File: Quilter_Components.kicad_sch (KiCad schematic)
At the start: 38 parts, among them J1 Conn_01x10_Male, J2 Conn_01x10_Male, J3 Conn_01x10_Male, J4 Eurorack_10_pin_power, U1 TL072, U2 TL074, U3 TL074, U4 TL074

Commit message: Draft of 8HP component PCB routed
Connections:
- net AUDIO_BUFF3: now also J1.3 (Pin_3); no longer J2.2 (Pin_2)
- net AUDIO_BUFF4: now also J2.5 (Pin_5); no longer J1.8 (Pin_8)
- net AUDIO_IN4: now also J3.1 (Pin_1); no longer J3.5 (Pin_5)
- net FREQ_CV1: now also J3.7 (Pin_7); no longer J3.6 (Pin_6)
- net FREQ_CV4: now also J3.6 (Pin_6); no longer J3.3 (Pin_3)
- net FREQ_POT: now also J3.5 (Pin_5); no longer J3.7 (Pin_7)
- net FREQ_V_OCT2: now also J1.7 (Pin_7); no longer J2.4 (Pin_4)
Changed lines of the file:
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@@
     (effects (font (size 1.27 1.27)) (justify right bottom))
   )
-  (label "FREQ_V_OCT2" (at 56.515 95.885 0)
+  (label "FREQ_V_OCT2" (at 29.21 103.505 0)
     (effects (font (size 1.27 1.27)) (justify left bottom))
   )
@@
     (effects (font (size 1.27 1.27)) (justify right bottom))
   )
-  (label "AUDIO_IN4" (at 88.9 97.155 0)
+  (label "AUDIO_IN4" (at 88.9 86.995 0)
     (effects (font (size 1.27 1.27)) (justify left bottom))
   )
@@
     (effects (font (size 1.27 1.27)) (justify right bottom))
   )
-  (label "FREQ_CV1" (at 88.9 99.695 0)
+  (label "FREQ_CV1" (at 88.9 102.235 0)
     (effects (font (size 1.27 1.27)) (justify left bottom))
   )
@@
     (effects (font (size 1.27 1.27)) (justify left bottom))
   )
-  (label "AUDIO_BUFF3" (at 56.515 90.805 0)
+  (label "AUDIO_BUFF3" (at 29.21 93.345 0)
     (effects (font (size 1.27 1.27)) (justify left bottom))
   )
@@
     (effects (font (size 1.27 1.27)) (justify right bottom))
   )
-  (label "AUDIO_BUFF4" (at 29.21 106.045 0)
+  (label "AUDIO_BUFF4" (at 56.515 98.425 0)
     (effects (font (size 1.27 1.27)) (justify left bottom))
   )
-  (label "FREQ_CV4" (at 88.9 92.075 0)
+  (label "FREQ_CV4" (at 88.9 99.695 0)
     (effects (font (size 1.27 1.27)) (justify left bottom))
   )
@@
     (effects (font (size 1.27 1.27)) (justify left bottom))
   )
-  (label "FREQ_POT" (at 88.9 102.235 0)
+  (label "FREQ_POT" (at 88.9 97.155 0)
     (effects (font (size 1.27 1.27)) (justify left bottom))
   )

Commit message: First draft routing of Controls PCB
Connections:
- net +12V: now also J2.1 (Pin_1)
- net -12V: now also J1.1 (Pin_1)
- net AUDIO_IN2: now also J2.10 (Pin_10); no longer J2.9 (Pin_9)
- net FREQ_POT_5V: now also J2.7 (Pin_7); no longer J2.10 (Pin_10)
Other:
- moved on the sheet: J3
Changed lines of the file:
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@@
     (effects (font (size 1.27 1.27)) (justify right bottom))
   )
-  (label "FREQ_POT_5V" (at 56.515 111.125 0)
+  (label "FREQ_POT_5V" (at 56.515 103.505 0)
     (effects (font (size 1.27 1.27)) (justify left bottom))
   )
@@
     (effects (font (size 1.27 1.27)) (justify left bottom))
   )
-  (label "AUDIO_IN3" (at 88.9 107.315 0)
+  (label "AUDIO_IN3" (at 86.995 108.585 0)
     (effects (font (size 1.27 1.27)) (justify left bottom))
   )
@@
     (effects (font (size 1.27 1.27)) (justify right bottom))
   )
-  (label "AUDIO_IN4" (at 88.9 86.995 0)
+  (label "AUDIO_IN4" (at 86.995 88.265 0)
     (effects (font (size 1.27 1.27)) (justify left bottom))
   )
@@
     (effects (font (size 1.27 1.27)) (justify right bottom))
   )
-  (label "FREQ_V_OCT4" (at 88.9 89.535 0)
-    (effects (font (size 1.27 1.27)) (justify left bottom))
-  )
-  (label "FREQ_CV3" (at 88.9 104.775 0)
+  (label "FREQ_V_OCT4" (at 86.995 90.805 0)
+    (effects (font (size 1.27 1.27)) (justify left bottom))
+  )
+  (label "FREQ_CV3" (at 86.995 106.045 0)
     (effects (font (size 1.27 1.27)) (justify left bottom))
   )
@@
     (effects (font (size 1.27 1.27)) (justify left bottom))
   )
-  (label "AUDIO_IN2" (at 56.515 108.585 0)
+  (label "AUDIO_IN2" (at 56.515 111.125 0)
     (effects (font (size 1.27 1.27)) (justify left bottom))
   )
@@
     (effects (font (size 1.27 1.27)) (justify right bottom))
   )
-  (label "FREQ_CV1" (at 88.9 102.235 0)
+  (label "FREQ_CV1" (at 86.995 103.505 0)
     (effects (font (size 1.27 1.27)) (justify left bottom))
   )
@@
     (effects (font (size 1.27 1.27)) (justify right bottom))
   )
-  (label "Q_POT" (at 88.9 94.615 0)
+  (label "Q_POT" (at 86.995 95.885 0)
     (effects (font (size 1.27 1.27)) (justify left bottom))
   )
@@
     (effects (font (size 1.27 1.27)) (justify left bottom))
   )
-  (label "FREQ_CV4" (at 88.9 99.695 0)
+  (label "FREQ_CV4" (at 86.995 100.965 0)
     (effects (font (size 1.27 1.27)) (justify left bottom))
   )
@@
     (effects (font (size 1.27 1.27)) (justify right bottom))
   )
-  (label "FREQ_V_OCT3" (at 88.9 109.855 0)
+  (label "FREQ_V_OCT3" (at 86.995 111.125 0)
     (effects (font (size 1.27 1.27)) (justify left bottom))
   )
@@
     (effects (font (size 1.27 1.27)) (justify left bottom))
   )
-  (label "FREQ_POT" (at 88.9 97.155 0)
+  (label "FREQ_POT" (at 86.995 98.425 0)
     (effects (font (size 1.27 1.27)) (justify left bottom))
   )
@@
     (pin "8")
   )
+  (symbol (lib_id "power:+12V") (at 56.515 88.265 270) (unit 1)
+    (in_bom yes) (on_board yes) (fields_autoplaced)
+    (property "Reference" "#PWR0110" (id 0) (at 52.705 88.265 0)
+      (effects (font (size 1.27 1.27)) hide)
+    )
+    (property "Value" "+12V" (id 1) (at 60.9143 88.2649 90)
+      (effects (font (size 1.27 1.27)) (justify left))
+    )
+    (property "Footprint" "" (id 2) (at 56.515 88.265 0)
+      (effects (font (size 1.27 1.27)) hide)
+    )
+    (property "Datasheet" "" (id 3) (at 56.515 88.265 0)
+      (effects (font (size 1.27 1.27)) hide)
+    )
+    (pin "1")
+  )
   (symbol (lib_id "Connector:TestPoint") (at 163.195 169.545 90) (unit 1)
     (in_bom yes) (on_board yes)
@@
     )
     (property "Datasheet" "~" (id 3) (at 163.195 164.465 0)
+      (effects (font (size 1.27 1.27)) hide)
+    )
+    (pin "1")
+  )
+  (symbol (lib_id "power:-12V") (at 29.21 88.265 270) (unit 1)
+    (in_bom yes) (on_board yes) (fields_autoplaced)
+    (property "Reference" "#PWR0109" (id 0) (at 31.75 88.265 0)
+      (effects (font (size 1.27 1.27)) hide)
+    )
+    (property "Value" "-12V" (id 1) (at 33.02 88.2649 90)
+      (effects (font (size 1.27 1.27)) (justify left))
+    )
+    (property "Footprint" "" (id 2) (at 29.21 88.265 0)
+      (effects (font (size 1.27 1.27)) hide)
+    )
+    (property "Datasheet" "" (id 3) (at 29.21 88.265 0)
       (effects (font (size 1.27 1.27)) hide)
     )
@@
   )
   (symbol (lib_id "Connector:Conn_01x10_Male") (at 51.435 98.425 0) (unit 1)
-    (in_bom yes) (on_board yes) (fields_autoplaced)
-    (property "Reference" "J2" (id 0) (at 52.07 82.55 0))
-    (property "Value" "Conn_01x10_Male" (id 1) (at 52.07 85.09 0))
+    (in_bom yes) (on_board yes)
+    (property "Reference" "J2" (id 0) (at 58.42 81.915 0))
+    (property "Value" "Conn_01x10_Male" (id 1) (at 59.055 85.09 0))
     (property "Footprint" "Connector_PinHeader_2.54mm:PinHeader_1x10_P2.54mm_Vertical" (id 2) (at 51.435 98.425 0)
       (effects (font (size 1.27 1.27)) hide)
@@
   )
   (symbol (lib_id "Connector:Conn_01x10_Male") (at 24.13 98.425 0) (unit 1)
-    (in_bom yes) (on_board yes) (fields_autoplaced)
-    (property "Reference" "J1" (id 0) (at 24.765 82.55 0))
-    (property "Value" "Conn_01x10_Male" (id 1) (at 24.765 85.09 0))
+    (in_bom yes) (on_board yes)
+    (property "Reference" "J1" (id 0) (at 27.94 81.915 0))
+    (property "Value" "Conn_01x10_Male" (id 1) (at 31.75 85.09 0))
     (property "Footprint" "Connector_PinHeader_2.54mm:PinHeader_1x10_P2.54mm_Vertical" (id 2) (at 24.13 98.425 0)
       (effects (font (size 1.27 1.27)) hide)
@@
     (pin "1")
   )
-  (symbol (lib_id "Connector:Conn_01x10_Male") (at 83.82 97.155 0) (unit 1)
-    (in_bom yes) (on_board yes) (fields_autoplaced)
-    (property "Reference" "J3" (id 0) (at 84.455 81.28 0))
-    (property "Value" "Conn_01x10_Male" (id 1) (at 84.455 83.82 0))
-    (property "Footprint" "Connector_PinHeader_2.54mm:PinHeader_1x10_P2.54mm_Vertical" (id 2) (at 83.82 97.155 0)
-      (effects (font (size 1.27 1.27)) hide)
-    )
-    (property "Datasheet" "~" (id 3) (at 83.82 97.155 0)
+  (symbol (lib_id "Connector:Conn_01x10_Male") (at 81.915 98.425 0) (unit 1)
+    (in_bom yes) (on_board yes)
+    (property "Reference" "J3" (id 0) (at 90.17 81.915 0))
+    (property "Value" "Conn_01x10_Male" (id 1) (at 90.17 84.455 0))
+    (property "Footprint" "Connector_PinHeader_2.54mm:PinHeader_1x10_P2.54mm_Vertical" (id 2) (at 81.915 98.425 0)
+      (effects (font (size 1.27 1.27)) hide)
+    )
+    (property "Datasheet" "~" (id 3) (at 81.915 98.425 0)
       (effects (font (size 1.27 1.27)) hide)
     )
@@
       (reference "#PWR0108") (unit 1) (value "GND") (footprint "")
     )
+    (path "/1aaa51bf-e78e-45fa-8100-3ef683a49ac4"
+      (reference "#PWR0109") (unit 1) (value "-12V") (footprint "")
+    )
+    (path "/0fd6de80-7cc0-4387-a408-b278fa25950a"
+      (reference "#PWR0110") (unit 1) (value "+12V") (footprint "")
+    )
     (path "/2c333ca4-0780-4b24-87eb-2f414d90e6bb"

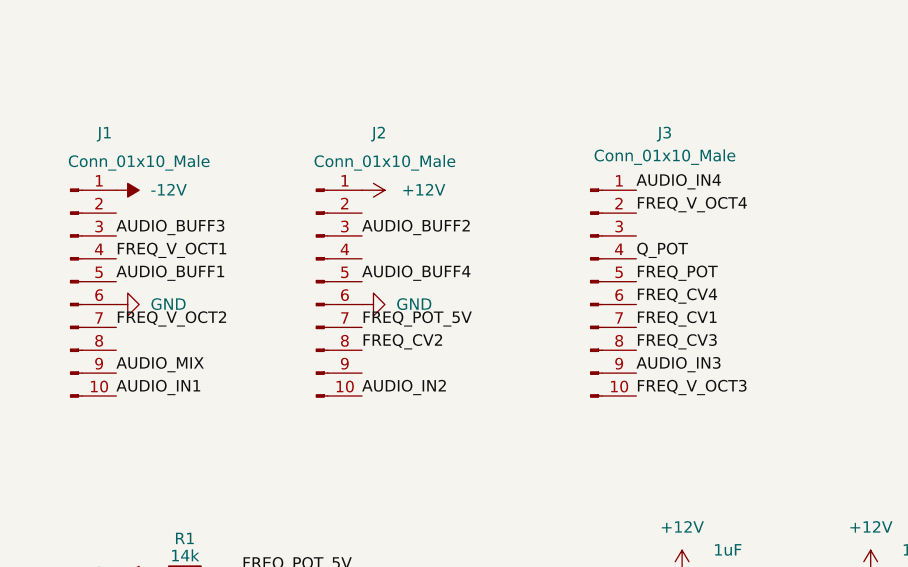
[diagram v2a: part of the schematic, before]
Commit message: Re-routed Controls board
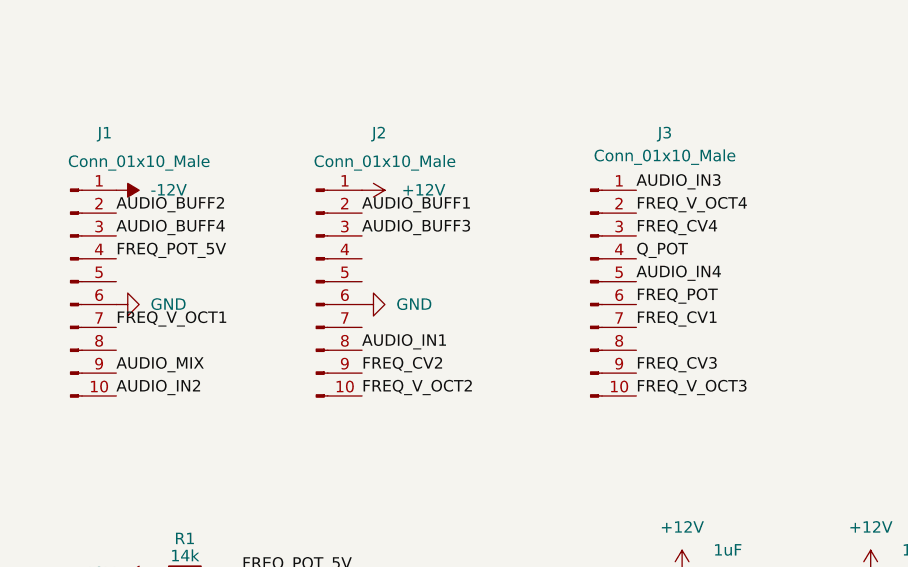
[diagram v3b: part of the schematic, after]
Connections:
- net AUDIO_BUFF1: now also J2.2 (Pin_2); no longer J1.5 (Pin_5)
- net AUDIO_BUFF2: now also J1.2 (Pin_2); no longer J2.3 (Pin_3)
- net AUDIO_BUFF3: now also J2.3 (Pin_3); no longer J1.3 (Pin_3)
- net AUDIO_BUFF4: now also J1.3 (Pin_3); no longer J2.5 (Pin_5)
- net AUDIO_IN1: now also J2.8 (Pin_8); no longer J1.10 (Pin_10)
- net AUDIO_IN2: now also J1.10 (Pin_10); no longer J2.10 (Pin_10)
- net AUDIO_IN3: now also J3.1 (Pin_1); no longer J3.9 (Pin_9)
- net AUDIO_IN4: now also J3.5 (Pin_5); no longer J3.1 (Pin_1)
- net FREQ_CV2: now also J2.9 (Pin_9); no longer J2.8 (Pin_8)
- net FREQ_CV3: now also J3.9 (Pin_9); no longer J3.8 (Pin_8)
- net FREQ_CV4: now also J3.3 (Pin_3); no longer J3.6 (Pin_6)
- net FREQ_POT: now also J3.6 (Pin_6); no longer J3.5 (Pin_5)
- net FREQ_POT_5V: now also J1.4 (Pin_4); no longer J2.7 (Pin_7)
- net FREQ_V_OCT1: now also J1.7 (Pin_7); no longer J1.4 (Pin_4)
- net FREQ_V_OCT2: now also J2.10 (Pin_10); no longer J1.7 (Pin_7)
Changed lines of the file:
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@@
     (effects (font (size 1.27 1.27)) (justify right bottom))
   )
-  (label "FREQ_POT_5V" (at 56.515 103.505 0)
+  (label "FREQ_POT_5V" (at 29.21 95.885 0)
     (effects (font (size 1.27 1.27)) (justify left bottom))
   )
@@
     (effects (font (size 1.27 1.27)) (justify right bottom))
   )
-  (label "FREQ_V_OCT2" (at 29.21 103.505 0)
+  (label "FREQ_V_OCT2" (at 56.515 111.125 0)
     (effects (font (size 1.27 1.27)) (justify left bottom))
   )
-  (label "AUDIO_IN3" (at 86.995 108.585 0)
+  (label "AUDIO_IN3" (at 86.995 88.265 0)
     (effects (font (size 1.27 1.27)) (justify left bottom))
   )
@@
     (effects (font (size 1.27 1.27)) (justify right bottom))
   )
-  (label "AUDIO_IN4" (at 86.995 88.265 0)
+  (label "AUDIO_IN4" (at 86.995 98.425 0)
     (effects (font (size 1.27 1.27)) (justify left bottom))
   )
@@
     (effects (font (size 1.27 1.27)) (justify left bottom))
   )
-  (label "FREQ_CV3" (at 86.995 106.045 0)
+  (label "FREQ_CV3" (at 86.995 108.585 0)
     (effects (font (size 1.27 1.27)) (justify left bottom))
   )
@@
     (effects (font (size 1.27 1.27)) (justify right bottom))
   )
-  (label "AUDIO_BUFF2" (at 56.515 93.345 0)
+  (label "AUDIO_BUFF2" (at 29.21 90.805 0)
     (effects (font (size 1.27 1.27)) (justify left bottom))
   )
@@
     (effects (font (size 1.27 1.27)) (justify right bottom))
   )
-  (label "AUDIO_BUFF1" (at 29.21 98.425 0)
+  (label "AUDIO_BUFF1" (at 56.515 90.805 0)
     (effects (font (size 1.27 1.27)) (justify left bottom))
   )
-  (label "AUDIO_IN2" (at 56.515 111.125 0)
+  (label "AUDIO_IN2" (at 29.21 111.125 0)
     (effects (font (size 1.27 1.27)) (justify left bottom))
   )
-  (label "FREQ_CV2" (at 56.515 106.045 0)
+  (label "FREQ_CV2" (at 56.515 108.585 0)
     (effects (font (size 1.27 1.27)) (justify left bottom))
   )
@@
     (effects (font (size 1.27 1.27)) (justify left bottom))
   )
-  (label "FREQ_V_OCT1" (at 29.21 95.885 0)
+  (label "FREQ_V_OCT1" (at 29.21 103.505 0)
     (effects (font (size 1.27 1.27)) (justify left bottom))
   )
@@
     (effects (font (size 1.27 1.27)) (justify left bottom))
   )
-  (label "AUDIO_BUFF3" (at 29.21 93.345 0)
+  (label "AUDIO_BUFF3" (at 56.515 93.345 0)
     (effects (font (size 1.27 1.27)) (justify left bottom))
   )
-  (label "AUDIO_IN1" (at 29.21 111.125 0)
+  (label "AUDIO_IN1" (at 56.515 106.045 0)
     (effects (font (size 1.27 1.27)) (justify left bottom))
   )
@@
     (effects (font (size 1.27 1.27)) (justify right bottom))
   )
-  (label "AUDIO_BUFF4" (at 56.515 98.425 0)
+  (label "AUDIO_BUFF4" (at 29.21 93.345 0)
     (effects (font (size 1.27 1.27)) (justify left bottom))
   )
-  (label "FREQ_CV4" (at 86.995 100.965 0)
+  (label "FREQ_CV4" (at 86.995 93.345 0)
     (effects (font (size 1.27 1.27)) (justify left bottom))
   )
@@
     (effects (font (size 1.27 1.27)) (justify left bottom))
   )
-  (label "FREQ_POT" (at 86.995 98.425 0)
+  (label "FREQ_POT" (at 86.995 100.965 0)
     (effects (font (size 1.27 1.27)) (justify left bottom))
   )

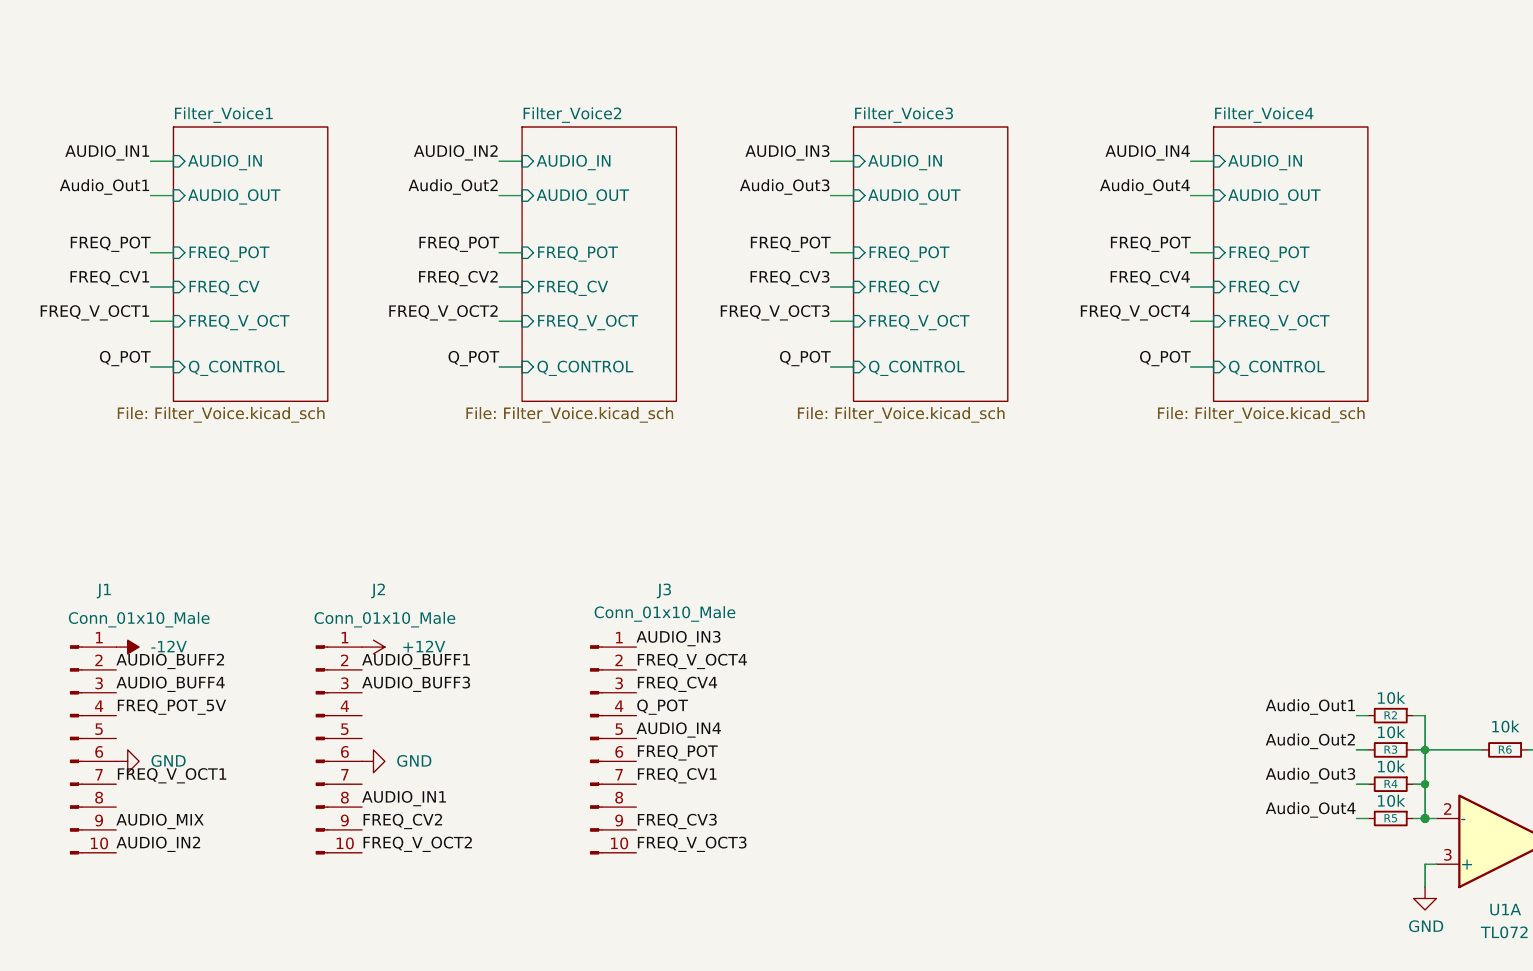
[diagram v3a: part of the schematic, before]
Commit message: Added all voice filter CV; panel draft done
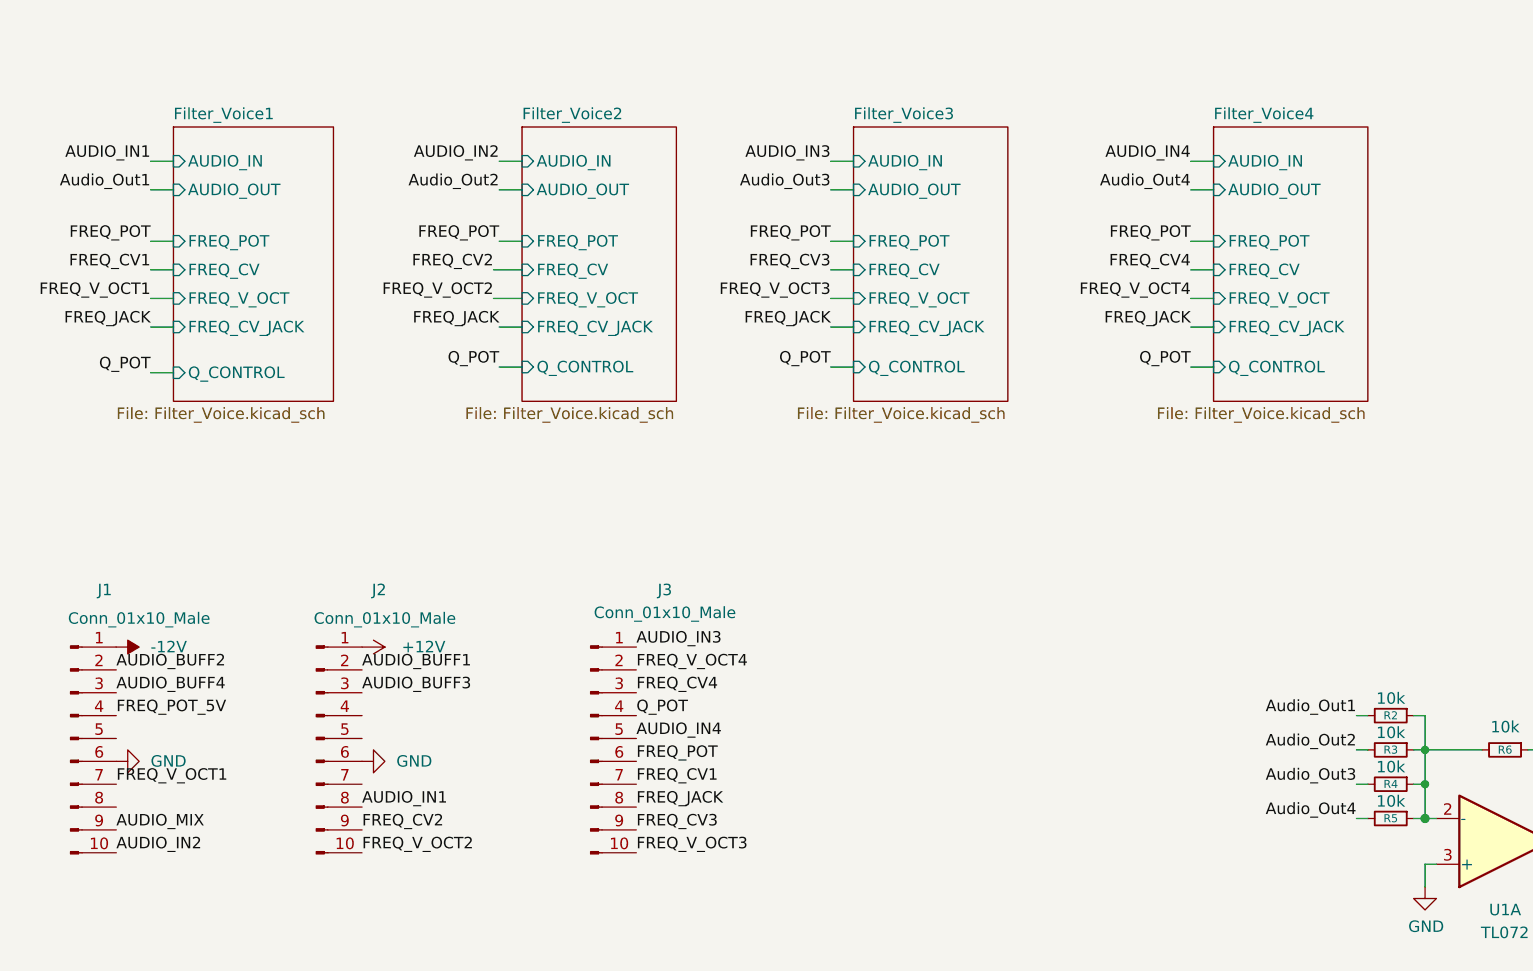
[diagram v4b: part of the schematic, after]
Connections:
- net FREQ_JACK: now reaches J3.8 (Pin_8)
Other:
- sheet Filter_Voice1 ports: added FREQ_CV_JACK; removed none
- sheet Filter_Voice2 ports: added FREQ_CV_JACK; removed none
- sheet Filter_Voice3 ports: added FREQ_CV_JACK; removed none
- sheet Filter_Voice4 ports: added FREQ_CV_JACK; removed none
